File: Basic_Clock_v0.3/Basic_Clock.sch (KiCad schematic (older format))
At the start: 30 parts, among them J1 Conn_01x04_Female, J2 Conn_01x04_Female, J4 Screw_Terminal_01x02, SW1 SW_Push_Reset, SW2 SW_Push, SW3 SW_Push, SW4 SW_Push, U1 LM317_TO-220, U2 ATmega328P-PU, Y1 16Mhz

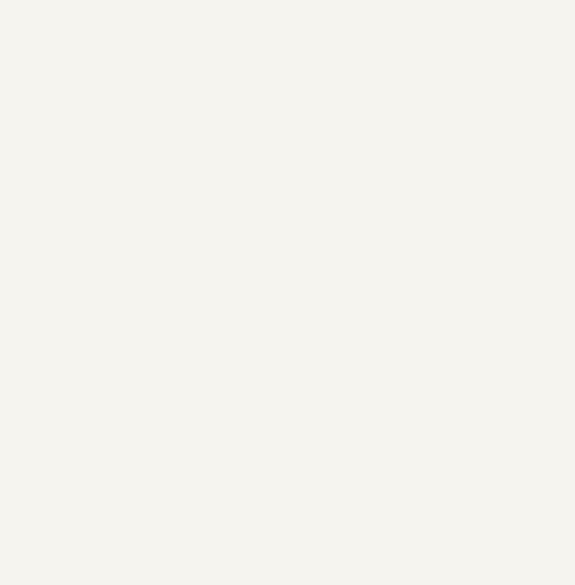
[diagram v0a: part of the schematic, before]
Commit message: New Testprogram Reorganized Folder
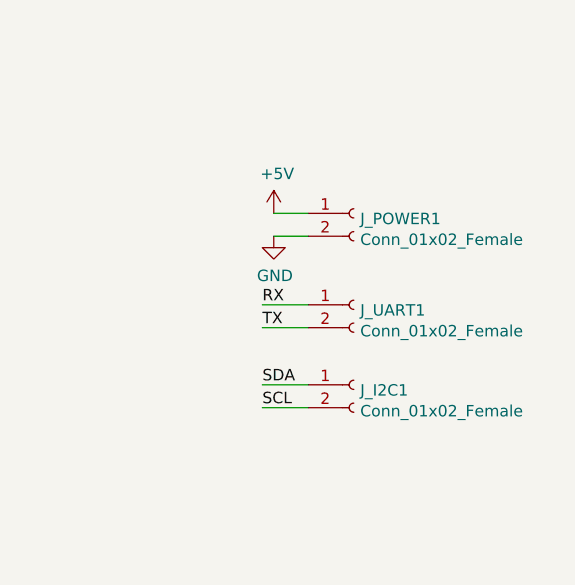
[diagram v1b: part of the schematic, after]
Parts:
- added J_I2C1, J_POWER1, J_UART1: Conn_01x02_Female, Connector THT:PinSocket_1x02_P2.54mm_Vertical, symbol Connector:Conn_01x02_Female
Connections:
- wire segments 99 -> 105
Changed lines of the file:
@@
 Wire Wire Line
 	6985 3685 6900 3685
+$Comp
+L Connector:Conn_01x02_Female J_POWER1
+U 1 1 5F941665
+P 9700 4250
+F 0 "J_POWER1" H 9728 4226 50  0000 L CNN
+F 1 "Conn_01x02_Female" H 9728 4135 50  0000 L CNN
+F 2 "Connector THT:PinSocket_1x02_P2.54mm_Vertical" H 9700 4250 50  0001 C CNN
+F 3 "~" H 9700 4250 50  0001 C CNN
+	1    9700 4250
+	1    0    0    -1
+$EndComp
+$Comp
+L Connector:Conn_01x02_Female J_UART1
+U 1 1 5F941F8B
+P 9700 4650
+F 0 "J_UART1" H 9728 4626 50  0000 L CNN
+F 1 "Conn_01x02_Female" H 9728 4535 50  0000 L CNN
+F 2 "Connector THT:PinSocket_1x02_P2.54mm_Vertical" H 9700 4650 50  0001 C CNN
+F 3 "~" H 9700 4650 50  0001 C CNN
+	1    9700 4650
+	1    0    0    -1
+$EndComp
+$Comp
+L Connector:Conn_01x02_Female J_I2C1
+U 1 1 5F942322
+P 9700 5000
+F 0 "J_I2C1" H 9728 4976 50  0000 L CNN
+F 1 "Conn_01x02_Female" H 9728 4885 50  0000 L CNN
+F 2 "Connector THT:PinSocket_1x02_P2.54mm_Vertical" H 9700 5000 50  0001 C CNN
+F 3 "~" H 9700 5000 50  0001 C CNN
+	1    9700 5000
+	1    0    0    -1
+$EndComp
+$Comp
+L power:GND #PWR0124
+U 1 1 5F942A97
+P 9350 4350
+F 0 "#PWR0124" H 9350 4100 50  0001 C CNN
+F 1 "GND" H 9355 4177 50  0000 C CNN
+F 2 "" H 9350 4350 50  0001 C CNN
+F 3 "" H 9350 4350 50  0001 C CNN
+	1    9350 4350
+	1    0    0    -1
+$EndComp
+$Comp
+L power:+5V #PWR0125
+U 1 1 5F942D77
+P 9350 4250
+F 0 "#PWR0125" H 9350 4100 50  0001 C CNN
+F 1 "+5V" H 9365 4423 50  0000 C CNN
+F 2 "" H 9350 4250 50  0001 C CNN
+F 3 "" H 9350 4250 50  0001 C CNN
+	1    9350 4250
+	1    0    0    -1
+$EndComp
+Wire Wire Line
+	9500 4250 9350 4250
+Wire Wire Line
+	9350 4350 9500 4350
+Wire Wire Line
+	9500 4650 9300 4650
+Wire Wire Line
+	9500 4750 9300 4750
+Text Label 9300 4650 0    50   ~ 0
+RX
+Text Label 9300 4750 0    50   ~ 0
+TX
+Wire Wire Line
+	9500 5000 9300 5000
+Wire Wire Line
+	9500 5100 9300 5100
+Text Label 9300 5000 0    50   ~ 0
+SDA
+Text Label 9300 5100 0    50   ~ 0
+SCL
 $EndSCHEMATC
